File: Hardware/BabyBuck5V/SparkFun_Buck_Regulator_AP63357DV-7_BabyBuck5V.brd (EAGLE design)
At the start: 15.9 x 13.2 mm, 32 parts, among them U1 AP63357

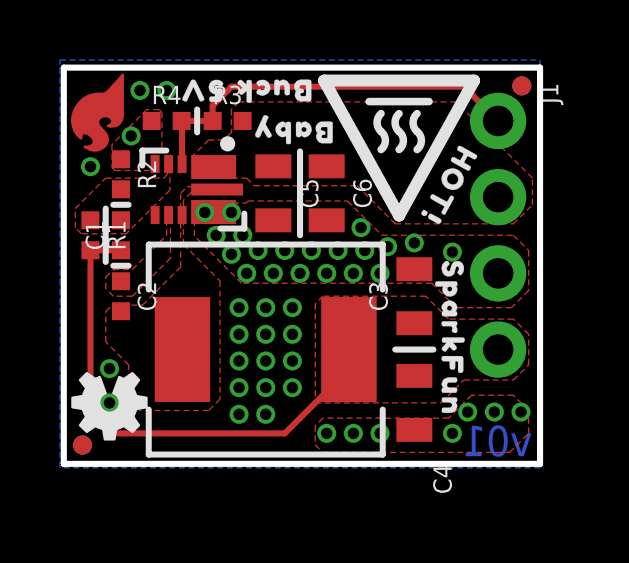
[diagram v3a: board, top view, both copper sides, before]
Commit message: Slight component shuffling in prep for protos.
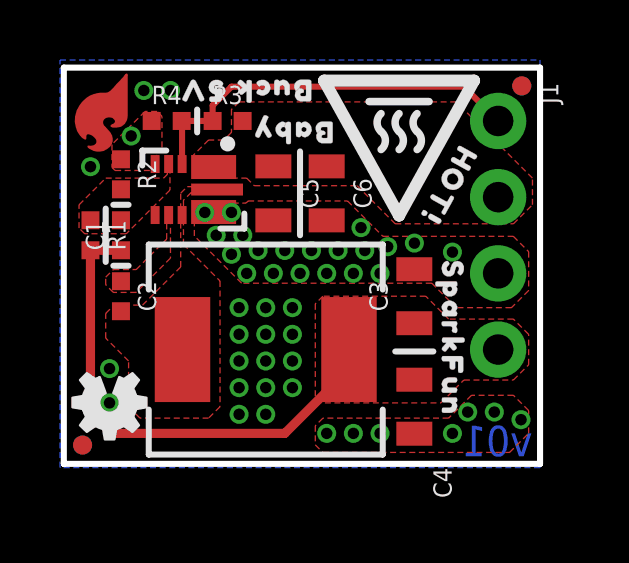
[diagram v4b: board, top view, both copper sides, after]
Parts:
- moved C4 0.13 mm to (11.7, 1.91)
- moved U$1 0.13 mm to (1.27, 11.7)
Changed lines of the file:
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@@
 <layers>
 <layer number="1" name="Top" color="4" fill="1" visible="yes" active="yes"/>
-<layer number="2" name="Route2" color="21" fill="1" visible="no" active="yes"/>
-<layer number="15" name="Route15" color="32" fill="1" visible="no" active="yes"/>
-<layer number="16" name="Bottom" color="1" fill="1" visible="no" active="yes"/>
+<layer number="2" name="Route2" color="21" fill="1" visible="yes" active="yes"/>
+<layer number="15" name="Route15" color="32" fill="1" visible="yes" active="yes"/>
+<layer number="16" name="Bottom" color="1" fill="1" visible="yes" active="yes"/>
 <layer number="17" name="Pads" color="2" fill="1" visible="yes" active="yes"/>
 <layer number="18" name="Vias" color="2" fill="1" visible="yes" active="yes"/>
@@
 <layer number="23" name="tOrigins" color="15" fill="1" visible="yes" active="yes"/>
 <layer number="24" name="bOrigins" color="15" fill="1" visible="yes" active="yes"/>
-<layer number="25" name="tNames" color="7" fill="1" visible="yes" active="yes"/>
+<layer number="25" name="tNames" color="7" fill="1" visible="no" active="yes"/>
 <layer number="26" name="bNames" color="7" fill="1" visible="no" active="yes"/>
 <layer number="27" name="tValues" color="7" fill="1" visible="no" active="yes"/>
@@
 <wire x1="4.445" y1="11.811" x2="4.445" y2="11.049" width="0.2032" layer="21"/>
 <wire x1="7.874" y1="10.414" x2="7.874" y2="7.62" width="0.2032" layer="21"/>
-<wire x1="11.049" y1="3.81" x2="12.319" y2="3.81" width="0.2032" layer="21"/>
+<wire x1="11.049" y1="3.7465" x2="12.319" y2="3.7465" width="0.2032" layer="21"/>
 <rectangle x1="1.143" y1="0.254" x2="11.303" y2="12.954" layer="30"/>
 <text x="15.621" y="0.254" size="1.016" layer="16" font="vector" ratio="15" rot="MR0">v01</text>
@@
 <attribute name="VALUE" x="12.573" y="5.588" size="0.6096" layer="27" font="vector" ratio="20" rot="R90" align="top-center"/>
 </element>
-<element name="C4" library="SparkFun-Capacitors" package="0805" value="22uF" x="11.684" y="2.032" smashed="yes" rot="R270">
-<attribute name="NAME" x="12.319" y="-0.508" size="0.6096" layer="25" font="vector" ratio="20" rot="R270" align="bottom-center"/>
-<attribute name="PROD_ID" value="CAP-14260" x="0.254" y="-37.338" size="1.778" layer="27" rot="R270" display="off"/>
-<attribute name="VALUE" x="10.795" y="2.032" size="0.6096" layer="27" font="vector" ratio="20" rot="R270" align="top-center"/>
+<element name="C4" library="SparkFun-Capacitors" package="0805" value="22uF" x="11.684" y="1.905" smashed="yes" rot="R270">
+<attribute name="NAME" x="12.319" y="-0.635" size="0.6096" layer="25" font="vector" ratio="20" rot="R270" align="bottom-center"/>
+<attribute name="PROD_ID" value="CAP-14260" x="0.254" y="-37.465" size="1.778" layer="27" rot="R270" display="off"/>
+<attribute name="VALUE" x="10.795" y="1.905" size="0.6096" layer="27" font="vector" ratio="20" rot="R270" align="top-center"/>
 </element>
 <element name="C6" library="SparkFun-Capacitors" package="0805" value="4.7uF" x="8.763" y="9.017" smashed="yes" rot="R270">
@@
 <attribute name="PROD_ID" value="VREG-" x="-26.162" y="28.194" size="1.778" layer="27" rot="R180" display="off"/>
 </element>
-<element name="U$1" library="SparkFun-Aesthetics" package="SFE_LOGO_FLAME_COPPER_EXPOSED_.1" value="" x="1.143" y="11.684" smashed="yes" rot="R180"/>
+<element name="U$1" library="SparkFun-Aesthetics" package="SFE_LOGO_FLAME_COPPER_EXPOSED_.1" value="" x="1.27" y="11.684" smashed="yes" rot="R180"/>
 <element name="U$8" library="SparkFun-Aesthetics" package="HIGH_TEMP_WARNING" value="" x="11.176" y="11.176" smashed="yes" rot="R180"/>
 <element name="U$6" library="output" package="BABY0" value="" x="7.62" y="11.049" smashed="yes" rot="R180"/>
@@
 <vertex x="3.53821875" y="9.12621875"/>
 <vertex x="2.0828" y="7.6708"/>
-<vertex x="0.5842" y="7.6708"/>
-<vertex x="0.381" y="7.874"/>
-<vertex x="0.381" y="8.509"/>
+<vertex x="0.695959375" y="7.6708"/>
+<vertex x="0.508" y="7.858759375"/>
+<vertex x="0.508" y="8.636"/>
 <vertex x="1.397" y="9.525"/>
 <vertex x="3.3274" y="9.525"/>
@@
 <vertex x="3.9878" y="7.3152"/>
 <vertex x="5.207" y="6.096"/>
-<vertex x="5.207" y="2.159"/>
-<vertex x="4.826" y="1.778"/>
-<vertex x="2.54" y="1.778"/>
-<vertex x="2.159" y="2.159"/>
-<vertex x="2.159" y="3.302"/>
-<vertex x="1.397" y="4.064"/>
-<vertex x="1.397" y="5.08"/>
-<vertex x="1.60781875" y="5.29081875"/>
+<vertex x="5.207" y="1.905"/>
+<vertex x="4.826" y="1.524"/>
+<vertex x="2.54" y="1.524"/>
+<vertex x="2.159" y="1.905"/>
+<vertex x="2.159" y="3.429"/>
+<vertex x="1.397" y="4.191"/>
+<vertex x="1.397" y="5.0139625"/>
+<vertex x="1.67385625" y="5.29081875"/>
 <vertex x="2.62381875" y="5.29081875"/>
 <vertex x="3.896359375" y="6.563359375"/>
@@
 <vertex x="3.556" y="8.509"/>
 <vertex x="3.556" y="6.858"/>
-<vertex x="2.286" y="5.588"/>
-<vertex x="1.651" y="5.588"/>
-<vertex x="1.397" y="5.842"/>
+<vertex x="2.413" y="5.715"/>
+<vertex x="1.651" y="5.715"/>
+<vertex x="1.397" y="5.969"/>
 <vertex x="1.397" y="6.223"/>
 <vertex x="1.651" y="6.477"/>
-<vertex x="2.286" y="6.477"/>
-<vertex x="3.429" y="7.62"/>
+<vertex x="2.413" y="6.477"/>
+<vertex x="3.429" y="7.493"/>
 <vertex x="3.429" y="8.509"/>
 </polygon>
@@
 <vertex x="6.144259375" y="8.763"/>
 <vertex x="9.456421875" y="8.763"/>
-<vertex x="10.599421875" y="7.62"/>
-<vertex x="14.986" y="7.62"/>
-<vertex x="15.494" y="7.112"/>
+<vertex x="10.63498125" y="7.584440625"/>
+<vertex x="14.983459375" y="7.584440625"/>
+<vertex x="15.494" y="7.0739"/>
 <vertex x="15.494" y="5.7785"/>
 <vertex x="14.9225" y="5.207"/>
@@
 <vertex x="3.09371875" y="10.373359375"/>
 <vertex x="3.27151875" y="10.551159375"/>
-<vertex x="3.27151875" y="11.71448125"/>
-<vertex x="3.175" y="11.811"/>
-<vertex x="2.771140625" y="11.811"/>
+<vertex x="3.27151875" y="11.58748125"/>
+<vertex x="3.1115" y="11.7475"/>
+<vertex x="2.707640625" y="11.7475"/>
 <vertex x="1.60528125" y="10.645140625"/>
 </polygon>
-<via x="3.429" y="12.446" extent="1-16" drill="0.381"/>
-<via x="2.54" y="12.446" extent="1-16" drill="0.381"/>
+<via x="3.556" y="12.446" extent="1-16" drill="0.381"/>
+<via x="2.667" y="12.446" extent="1-16" drill="0.381"/>
 <via x="2.245359375" y="10.92961875" extent="1-16" drill="0.381"/>
 <via x="0.889" y="9.906" extent="1-16" drill="0.381"/>
@@
 <via x="9.906" y="7.874" extent="1-16" drill="0.381"/>
 <via x="10.795" y="7.239" extent="1-16" drill="0.381"/>
-<via x="11.684" y="7.366" extent="1-16" drill="0.381"/>
+<via x="11.686540625" y="7.35838125" extent="1-16" drill="0.381"/>
 <via x="12.954" y="7.058659375" extent="1-16" drill="0.381"/>
 <via x="1.524" y="3.175" extent="1-16" drill="0.381"/>
@@
 <via x="12.954" y="1.016" extent="1-16" drill="0.381"/>
 <via x="14.351" y="1.7272" extent="1-16" drill="0.381"/>
-<via x="15.24" y="1.7272" extent="1-16" drill="0.381"/>
+<via x="15.24" y="1.4732" extent="1-16" drill="0.381"/>
 <polygon width="0.2032" layer="1" thermals="no" rank="2">
 <vertex x="8.636" y="0.381"/>
@@
 <contactref element="C5" pad="1"/>
 <contactref element="J1" pad="2"/>
-<polygon width="0.2032" layer="1" thermals="no" rank="2">
+<polygon width="0.2032" layer="1" isolate="0.2032" thermals="no" rank="2">
 <vertex x="4.318" y="9.525"/>
 <vertex x="6.096" y="9.525"/>
@@
 <vertex x="15.494" y="4.318"/>
 </polygon>
-<wire x1="9.506" y1="3.81" x2="9.506" y2="3.156" width="0.2032" layer="1"/>
-<wire x1="9.506" y1="3.156" x2="7.366" y2="1.016" width="0.2032" layer="1"/>
-<wire x1="7.366" y1="1.016" x2="1.651" y2="1.016" width="0.2032" layer="1"/>
-<wire x1="1.651" y1="1.016" x2="0.889" y2="1.778" width="0.2032" layer="1"/>
-<wire x1="0.889" y1="1.778" x2="0.889" y2="7.12" width="0.2032" layer="1"/>
-<wire x1="0.889" y1="7.12" x2="1.905" y2="7.12" width="0.2032" layer="1"/>
+<wire x1="9.506" y1="3.81" x2="9.506" y2="3.156" width="0.3048" layer="1"/>
+<wire x1="9.506" y1="3.156" x2="7.366" y2="1.016" width="0.3048" layer="1"/>
+<wire x1="7.366" y1="1.016" x2="1.651" y2="1.016" width="0.3048" layer="1"/>
+<wire x1="1.651" y1="1.016" x2="0.889" y2="1.778" width="0.3048" layer="1"/>
+<wire x1="0.889" y1="1.778" x2="0.889" y2="7.12" width="0.3048" layer="1"/>
+<wire x1="0.889" y1="7.12" x2="1.905" y2="7.12" width="0.3048" layer="1"/>
 </signal>
 </signals>
